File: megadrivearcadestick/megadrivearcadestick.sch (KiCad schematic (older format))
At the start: 26 parts

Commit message: Better schematics
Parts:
- added J14: Up GND, symbol Connector:Conn_01x01_Female
- added J16: Down GND, symbol Connector:Conn_01x01_Female
- J1: renamed from J?; value Conn_01x01_Female -> Left GND
- J15: renamed from Down; value Conn_01x01_Female -> Down
- J2: renamed from J?; value Conn_01x01_Female -> Right GND
- J3: renamed from J?; value Conn_01x01_Female -> A GND
- J4: renamed from J?; value Conn_01x01_Female -> B GND
- J5: renamed from J?; value Conn_01x01_Female -> C GND
- J6: renamed from J?; value Conn_01x01_Female -> Start GND
- gave numbers to parts that had none: 6
- renumbered Up to J13
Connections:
- net GND: now also J?.8
- net at C1.1, R1.1, R2.1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: now also J?.5
- net at J12.1 (Pin_1), R8.2: now also U?.14 (I0d)
- net at J11.1 (Pin_1), R7.2: now also U?.13 (I1d)
- net at J10.1 (Pin_1), R6.2: now also U?.10 (I1c)
- net at J9.1 (Pin_1), R5.2: now also U?.11 (I0c)
- net at J8.1 (Pin_1), R4.2: now also U?.6 (I1b)
- net at J7.1 (Pin_1), R3.2: now also U?.3 (I1a)
- net at J13.1 (Pin_1), R2.2: now also J?.1
- net at J15.1 (Pin_1), R1.2: now also J?.2
- net at U?.12 (Zd): now also J?.9
- net at U?.4 (Za): now also J?.3
- net at U?.7 (Zb): now also J?.4
- net at U?.9 (Zc): now also J?.6
- net at J1.1 (Pin_1): now also J2.1 (Pin_1), J3.1 (Pin_1), J4.1 (Pin_1), J5.1 (Pin_1), J6.1 (Pin_1), J14.1 (Pin_1), J16.1 (Pin_1)
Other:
- moved on the sheet: J10, J11, J12, J13, J15, J7, J8, J9

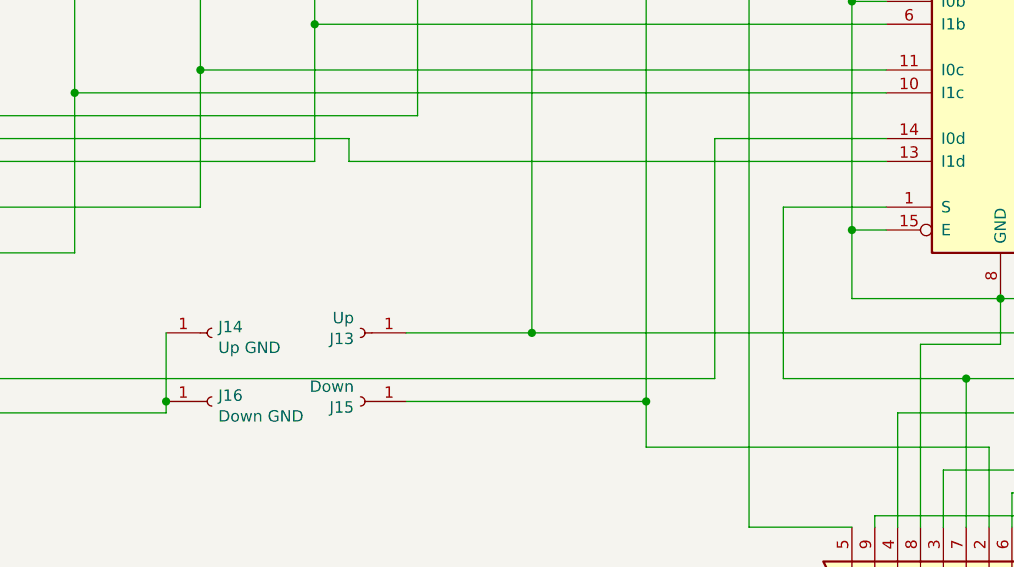
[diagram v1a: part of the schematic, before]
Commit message: Missing gnd
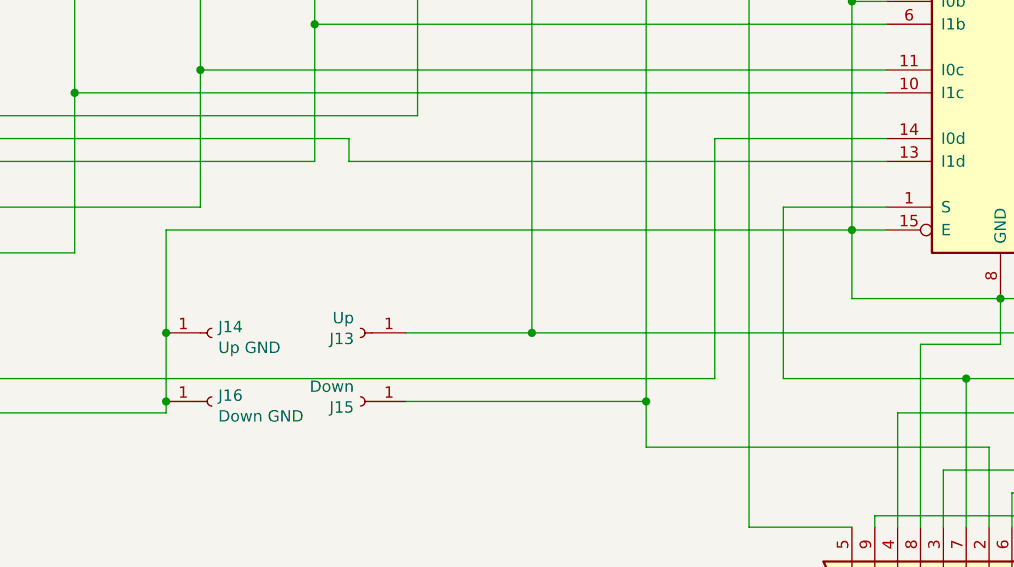
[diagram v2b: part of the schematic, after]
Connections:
- net GND: now also J1.1 (Pin_1), J14.1 (Pin_1), J16.1 (Pin_1), J2.1 (Pin_1), J3.1 (Pin_1), J4.1 (Pin_1), J5.1 (Pin_1), J6.1 (Pin_1)
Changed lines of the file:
@@
 Wire Wire Line
 	3300 3850 3300 3900
+Wire Wire Line
+	6300 3100 3300 3100
+Wire Wire Line
+	3300 3100 3300 3550
+Connection ~ 3300 3550
 $EndSCHEMATC
